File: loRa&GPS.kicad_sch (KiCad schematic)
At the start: 21 parts, among them SW3 RESET, SW4 RESET

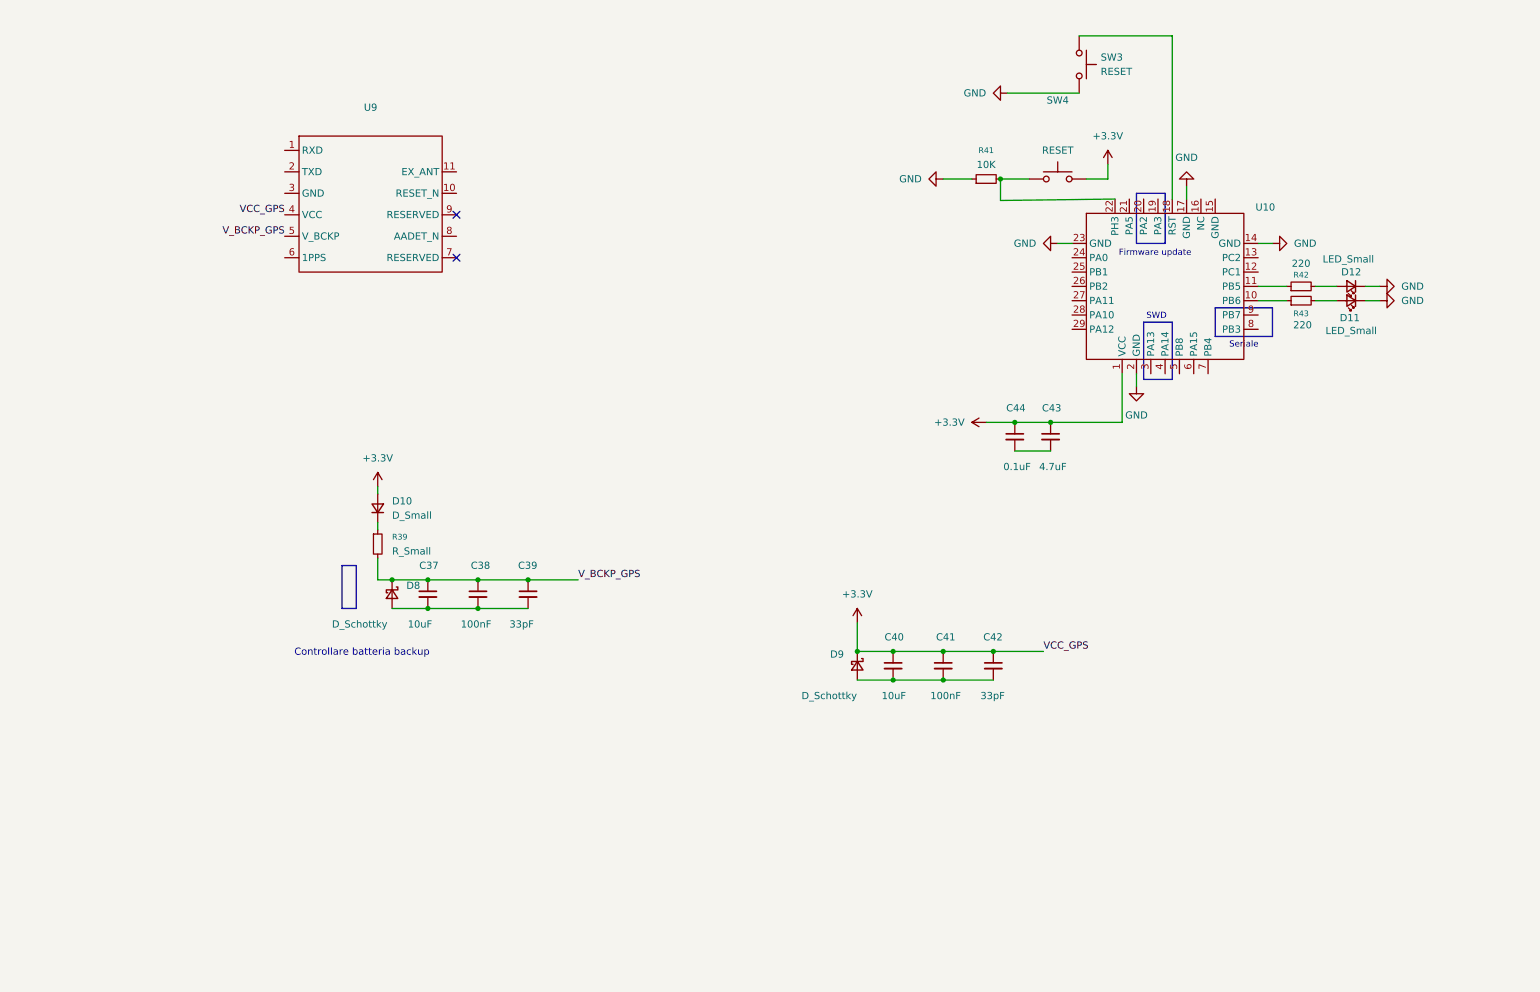
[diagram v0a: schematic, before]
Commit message: Comunicazione Pico - GPS/Radio
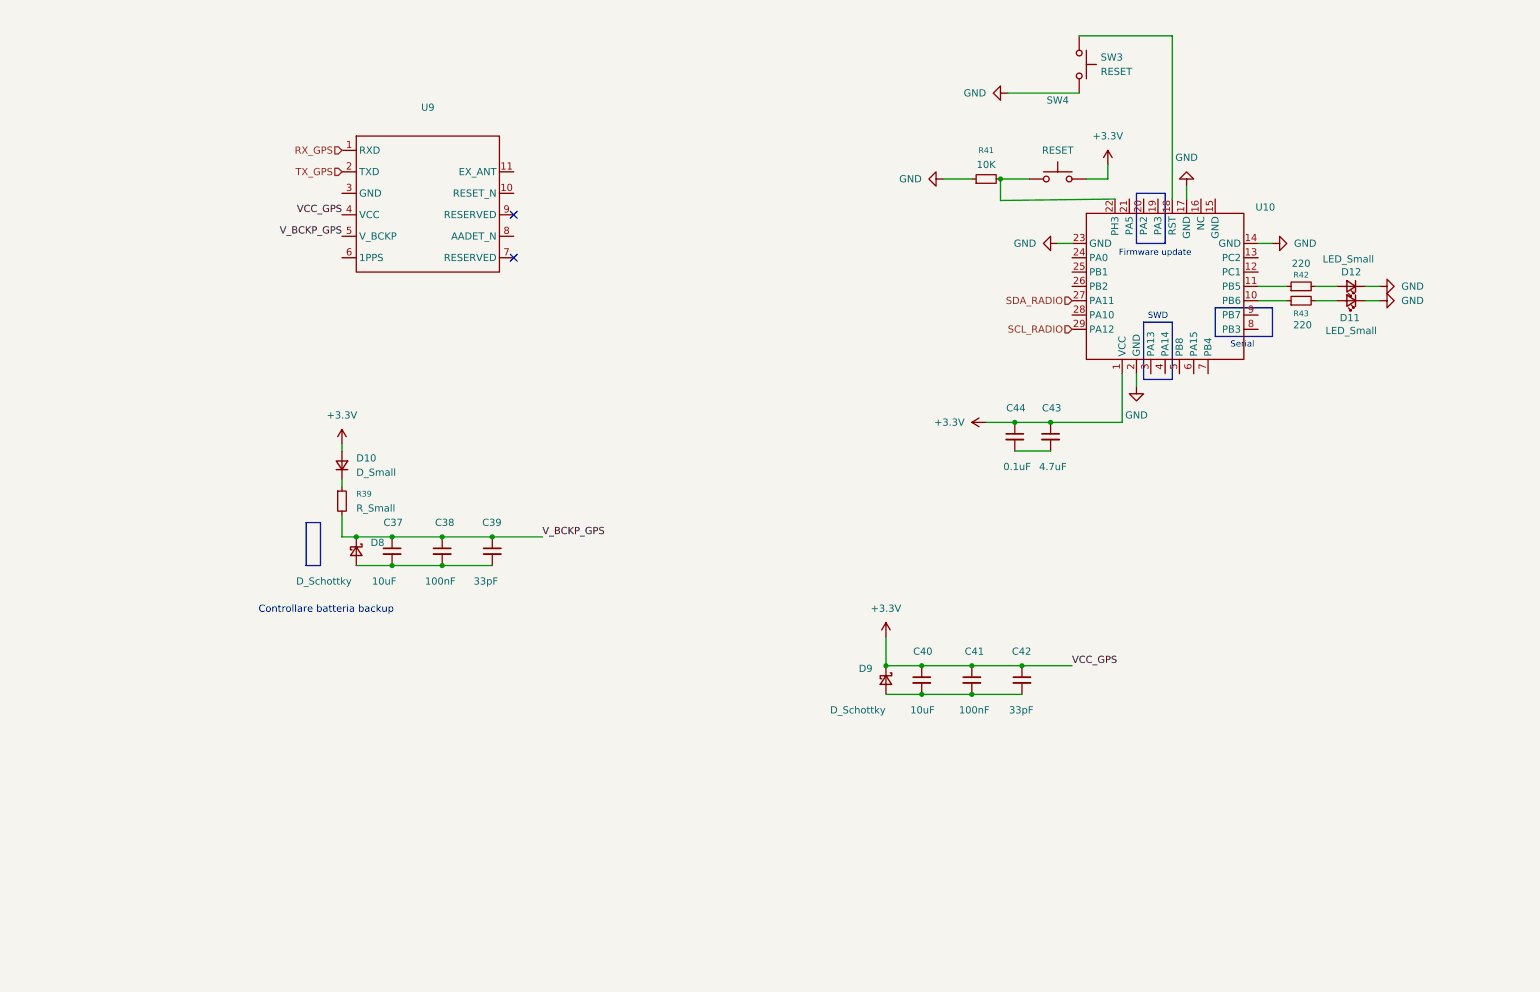
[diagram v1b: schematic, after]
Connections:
- net SDA_RADIO: now reaches U10.27 (PA11)
- net SCL_RADIO: now reaches U10.29 (PA12)
- net RX_GPS: now reaches U9.1 (RXD)
- net TX_GPS: now reaches U9.2 (TXD)
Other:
- note added: "Serial"
- note removed: "Seriale"
- moved on the sheet: C37, C38, C39, C40, C41, C42, D10, D8, D9, R39, U9

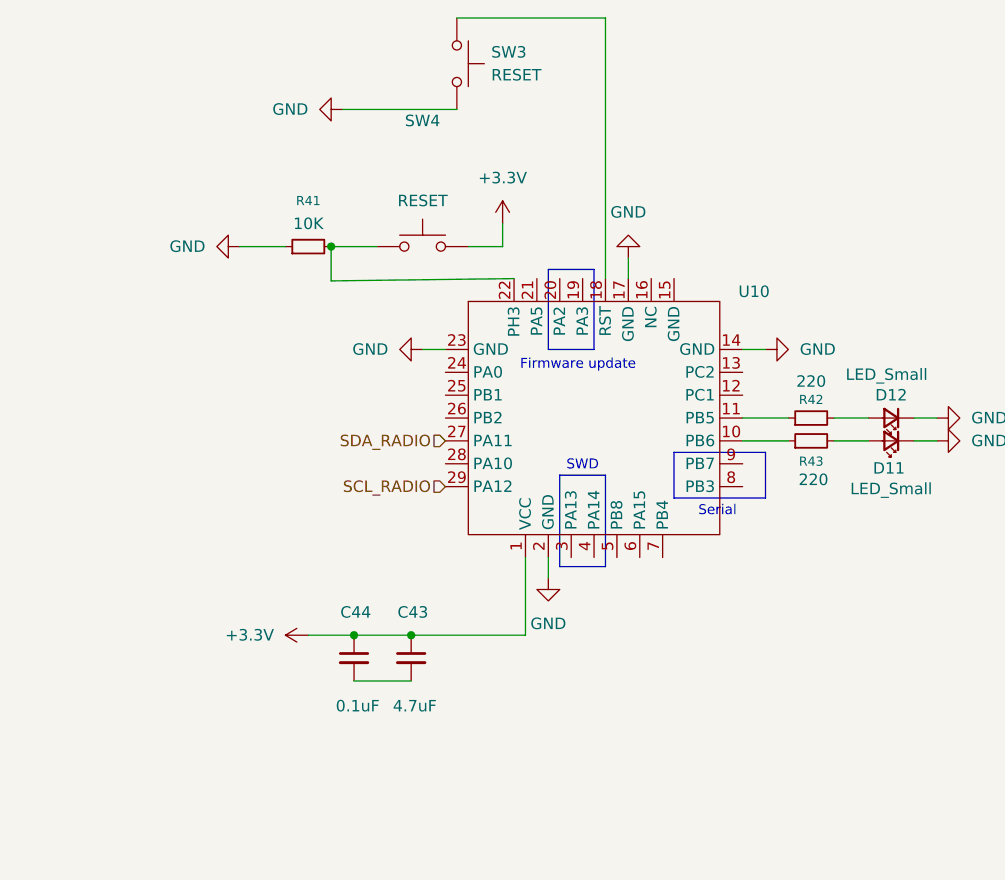
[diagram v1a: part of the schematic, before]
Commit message: Lora radio and gps small additions
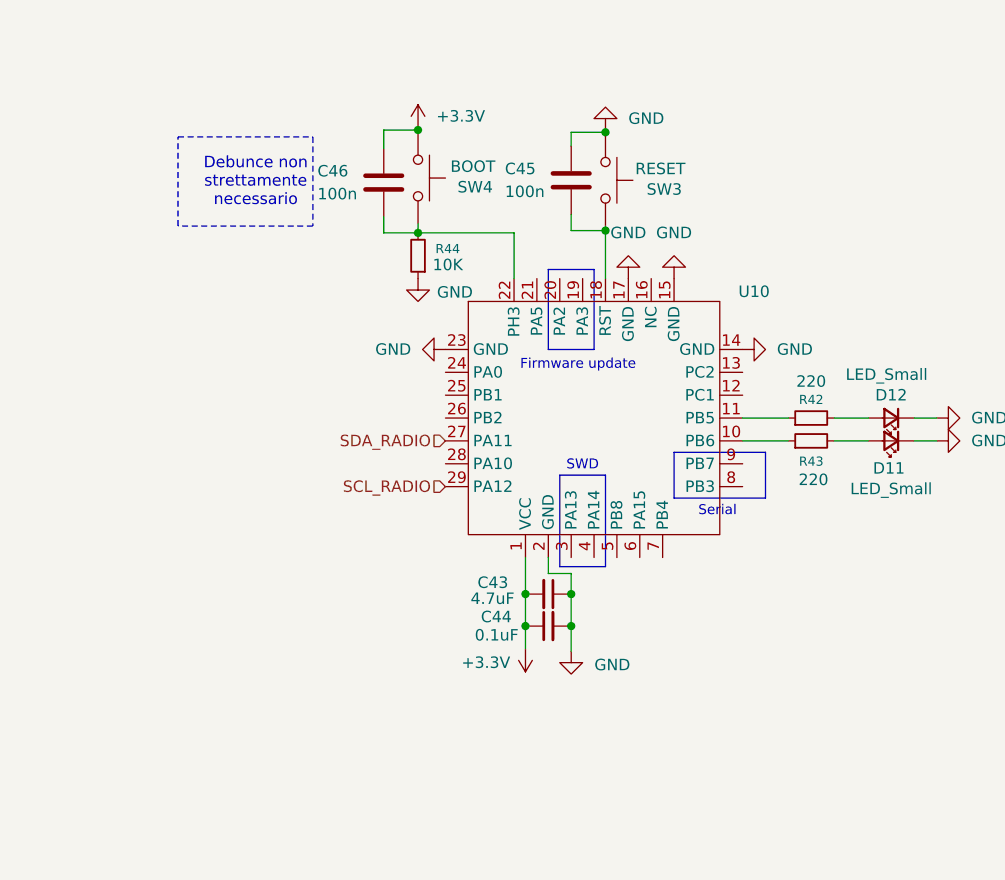
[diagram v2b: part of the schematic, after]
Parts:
- removed R41: 10K, symbol Device:R_Small
- added C45, C46: 100n, Capacitor_SMD:C_0603_1608Metric_Pad1.08x0.95mm_HandSolder, symbol Device:C
- added R44: 10K, Resistor_SMD:R_0603_1608Metric_Pad0.98x0.95mm_HandSolder, symbol Device:R_Small
- C37, C38, C39, C40, C41, C42, C43, C44: footprint (none) -> Capacitor_SMD:C_0603_1608Metric_Pad1.08x0.95mm_HandSolder
- R39, R42, R43: footprint (none) -> Resistor_SMD:R_0603_1608Metric_Pad0.98x0.95mm_HandSolder
- SW4: value RESET -> BOOT
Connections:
- net +3.3V: now also C43.2, SW4.1, C46.1; no longer C43.1, SW4.2
- net GND: now also C43.1, C44.2, SW3.1, U10.15 (GND), C45.1, R44.1; no longer SW3.2
- net at U10.22 (PH3): now also SW4.2, C46.2, R44.2; no longer SW4.1
- net at U10.18 (RST): now also SW3.2, C45.2; no longer SW3.1
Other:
- note added: "Debunce non strettamente necessario"
- moved on the sheet: C43, C44, SW3, SW4

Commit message: Corrections
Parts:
- U10: value ~ -> RC-WLE5-434
- U9: value ~ -> Quectel L86
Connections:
- net GND: now also C37.2, C38.2, C39.2, C40.2, C41.2, C42.2, D8.2 (A), D9.2 (A), U9.3 (GND)
- net +3.3V renamed +3V3
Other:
- note added: "Schottky o Zener??"
- moved on the sheet: C37, C38, C39, C40, C41, C42, C43, C44, C45, C46, D10, D11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

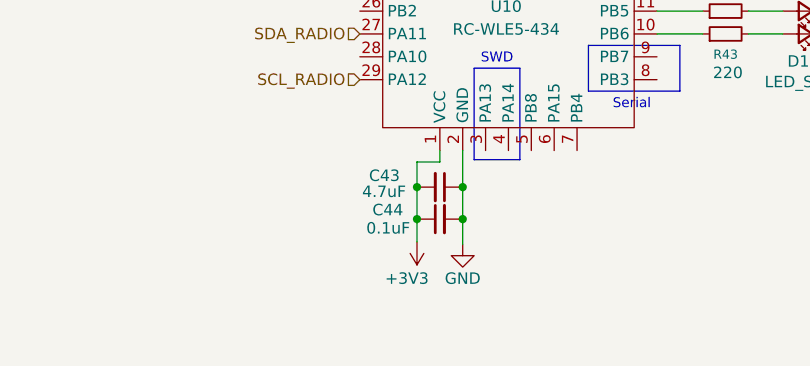
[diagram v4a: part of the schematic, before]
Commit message: RC-WLE5-434 aggiunta induttanza
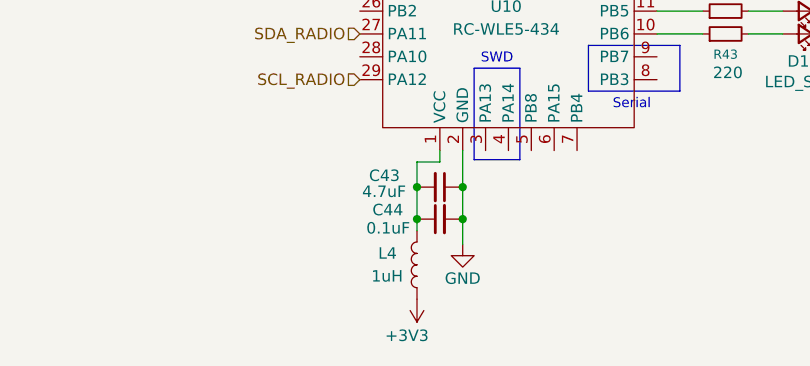
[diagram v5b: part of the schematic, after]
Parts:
- added L4: 1uH, symbol Device:L
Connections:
- net +3V3: now also L4.1; no longer C43.2, C44.1, U10.1 (VCC)
- new net: C43.2, C44.1, L4.2, U10.1 (VCC)
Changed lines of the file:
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@@
 	(wire
 		(pts
-			(xy 212.852 119.634) (xy 212.852 122.174)
+			(xy 212.852 119.634) (xy 212.852 120.904)
 		)
 		(stroke
@@
 	(symbol
 		(lib_id "power:+3.3V")
-		(at 212.852 122.174 180)
+		(at 212.852 128.524 180)
 		(unit 1)
 		(exclude_from_sim no)
@@
 		(dnp no)
 		(property "Reference" "#PWR0109"
-			(at 212.852 118.364 0)
+			(at 212.852 124.714 0)
 			(effects
 				(font
@@
 		)
 		(property "Value" "+3V3"
-			(at 209.296 126.238 0)
+			(at 209.296 132.588 0)
 			(effects
 				(font
@@
 		)
 		(property "Footprint" ""
-			(at 212.852 122.174 0)
+			(at 212.852 128.524 0)
 			(effects
 				(font
@@
 		)
 		(property "Datasheet" ""
-			(at 212.852 122.174 0)
+			(at 212.852 128.524 0)
 			(effects
 				(font
@@
 		)
 		(property "Description" "Power symbol creates a global label with name \"+3V3\""
-			(at 212.852 122.174 0)
+			(at 212.852 128.524 0)
 			(effects
 				(font
@@
 					(unit 1)
 				)
+			)
+		)
+	)
+	(symbol
+		(lib_id "Device:L")
+		(at 212.852 124.714 180)
+		(unit 1)
+		(exclude_from_sim no)
+		(in_bom yes)
+		(on_board yes)
+		(dnp no)
+		(property "Reference" "L4"
+			(at 208.534 123.444 0)
+			(effects
+				(font
+					(size 1.27 1.27)
+				)
+				(justify right)
+			)
+		)
+		(property "Value" "1uH"
+			(at 207.772 125.984 0)
+			(effects
+				(font
+					(size 1.27 1.27)
+				)
+				(justify right)
+			)
+		)
+		(property "Footprint" ""
+			(at 212.852 124.714 0)
+			(effects
+				(font
+					(size 1.27 1.27)
+				)
+				(hide yes)
+			)
+		)
+		(property "Datasheet" "~"
+			(at 212.852 124.714 0)
+			(effects
+				(font
+					(size 1.27 1.27)
+				)
+				(hide yes)
+			)
+		)
+		(property "Description" "Inductor"
+			(at 212.852 124.714 0)
+			(effects
+				(font
+					(size 1.27 1.27)
+				)
+				(hide yes)
+			)
+		)
+		(pin "2"
+		)
+		(pin "1"
+		)
+		(instances
+			(project ""
+				(path "/105f6e80-8e20-4d56-8eb3-6fa826818670/41f4c21a-5a60-4aaf-8b8a-29c50dd243d1"
+					(reference "L4")
+					(unit 1)
+				)

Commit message: New GPS and sensors
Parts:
- removed C37, C40: 10uF, Capacitor_SMD:C_0603_1608Metric_Pad1.08x0.95mm_HandSolder, symbol Device:C_Small
- removed C38, C41: 100nF, Capacitor_SMD:C_0603_1608Metric_Pad1.08x0.95mm_HandSolder, symbol Device:C_Small
- removed C39, C42: 33pF, Capacitor_SMD:C_0603_1608Metric_Pad1.08x0.95mm_HandSolder, symbol Device:C_Small
- removed D10: D_Small, symbol Device:D_Small
- removed D9: D_Schottky, SDM2U30CSP:SDM2U30CSP, symbol Device:D_Schottky_Small
- removed R39: R_Small, Resistor_SMD:R_0603_1608Metric_Pad0.98x0.95mm_HandSolder, symbol Device:R_Small
- removed U9: Quectel L86, symbol LC68G:LC68G
- added BT1: Battery_Cell, symbol Device:Battery_Cell
- added C37: 100nF, symbol Device:C
- added R39: 47k, symbol Device:R
- added U9: TESEO-LIV4F, TESEO_LIV4F:XCVR_TESEO-LIV4F, symbol TESEO-LIV4F:TESEO-LIV4F
- D8: value D_Schottky -> D_Schottky_Small; footprint SDM2U30CSP:SDM2U30CSP -> (none)
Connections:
- net +3V3: now also D8.2 (A), U9.8 (VCC)
- net GND: now also BT1.2 (-), C37.2, U9.1 (GND), U9.10 (GND_RF), U9.12 (GND_RF__1); no longer D8.2 (A)
- net RX_GPS: now also U9.3 (UART-RX)
- net TX_GPS: now also U9.2 (UART-TX)
- net V_BCKP_GPS: no longer names the net of D8.1 (K)
- net V_BCKP_GPS: now also R39.1
- new net: BT1.1 (+), C37.1, R39.2, U9.6 (VBAT)
- no-connect marks 2 -> 5
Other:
- note removed: "Controllare batteria backup"
- note removed: "Schottky o Zener??"

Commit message: GPS
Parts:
- added AE1: Antenna_Shield, symbol Device:Antenna_Shield
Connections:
- net GND: now also AE1.2 (Shield)
- net at U9.11 (RF_IN): now also AE1.1 (A)
- no-connect marks 5 -> 6
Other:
- moved on the sheet: C43, C44, C45, C46, D11, D12, L4, R42, R43, R44, SW3, SW4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

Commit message: LIV5
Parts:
- removed C43: 4.7uF, Capacitor_SMD:C_0603_1608Metric_Pad1.08x0.95mm_HandSolder, symbol Device:C_Small
- removed C44: 0.1uF, Capacitor_SMD:C_0603_1608Metric_Pad1.08x0.95mm_HandSolder, symbol Device:C_Small
- removed C45, C46: 100n, Capacitor_SMD:C_0603_1608Metric_Pad1.08x0.95mm_HandSolder, symbol Device:C
- removed D11, D12: LED_Small, LED_SMD:LED_0603_1608Metric, symbol Device:LED_Small
- removed L4: 1uH, symbol Device:L
- removed R42, R43: 220, Resistor_SMD:R_0603_1608Metric_Pad0.98x0.95mm_HandSolder, symbol Device:R_Small
- removed R44: 10K, Resistor_SMD:R_0603_1608Metric_Pad0.98x0.95mm_HandSolder, symbol Device:R_Small
- removed SW3: RESET, TSB008:TSB008, symbol Switch:SW_Push
- removed SW4: BOOT, TSB008:TSB008, symbol Switch:SW_Push
- removed U10: RC-WLE5-434, rc-wle5:RC-WLE5-XXX, symbol rc-wle5:rc-wle5-434
- added C25, C26, C40: 100nF, Capacitor_SMD:C_0603_1608Metric_Pad1.08x0.95mm_HandSolder, symbol Device:C
- added C39: 10nF, Capacitor_SMD:C_0603_1608Metric_Pad1.08x0.95mm_HandSolder, symbol Device:C
- added J4: Conn_Coaxial, sma_connector:SMA_EDGE__UFL, symbol Connector:Conn_Coaxial
- added U10: RAK3172, ul_RAK3172:RAK3172_RAK, symbol ul_RAK3172:RAK3172
- added U3: STA8135GA, footprints:TFBGA160_7X11X1p2_STM, symbol 2025-11-15_15-30-48:STA8135GA
- C37: footprint (none) -> Capacitor_SMD:C_0603_1608Metric_Pad1.08x0.95mm_HandSolder
- R39: footprint (none) -> Resistor_SMD:R_0603_1608Metric_Pad0.98x0.95mm_HandSolder
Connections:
- net +3V3: now also C26.1, C39.1, C40.1, U10.24 (VDD), U3.A5 (LDO_IN_3V3_1V8_0)
- net GND: now also C25.1, C26.2, C39.2, C40.2, J4.2 (Ext), U10.11 (GND), U10.17 (GND), U10.18 (GND), U10.23 (GND), U10.28 (GND), U3.B4 (GND_0), U3.B5 (RF_GND_0), U3.B6 (RF_GND_0), U3.B7 (RF_GND_0), U3.B8 (RF_GND_0), U3.B9 (RF_GND_0), U3.C4 (GND_0), U3.D3 (GND_0), U3.D5 (GND_0), U3.E3 (GND), U3.E4 (GND), U3.F2 (GND), U3.F8 (GND), U3.G2 (GND_PMU)
- net SCL_RADIO: now also U10.9 (PA12/I2C_SCL)
- net SDA_RADIO: now also U10.10 (PA11/I2C_SDA)
- new net: C25.2, U3.A4 (LDO_RF_OUT_1V1_0), U3.A9 (LNA_VCC_0)
- new net ANT: J4.1 (In), U10.12 (RF)
- no-connect marks 6 -> 19
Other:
- note removed: "Debunce non strettamente necessario"
- note removed: "Firmware update"
- note removed: "SWD"
- note removed: "Serial"
- moved on the sheet: AE1, BT1, C37, D8, R39, U9
